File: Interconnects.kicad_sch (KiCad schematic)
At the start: 8 parts, among them J101 KLDX-0202-B, J102 EBWA-02-B, J103 EBWA-02-B, J104 KLDX-0202-B

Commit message: fix: bom improvements & more notes
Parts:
- TP101, TP104: footprint TestPoint:TestPoint_THTPad_2.0x2.0mm_Drill1.0mm -> RD-Testpoints:TestPoint_THTPad_1.5x1.5mm_Drill0.7mm
- TP102, TP103: footprint TestPoint:TestPoint_Pad_D1.5mm -> RD-Testpoints:TestPoint_Pad_D1.5mm
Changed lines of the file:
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@@
 			)
 		)
-		(property "Footprint" "TestPoint:TestPoint_THTPad_2.0x2.0mm_Drill1.0mm"
+		(property "Footprint" "RD-Testpoints:TestPoint_THTPad_1.5x1.5mm_Drill0.7mm"
 			(at 177.8 88.9 0)
 			(effects
@@
 			)
 		)
-		(property "Footprint" "TestPoint:TestPoint_Pad_D1.5mm"
+		(property "Footprint" "RD-Testpoints:TestPoint_Pad_D1.5mm"
 			(at 133.35 73.66 0)
 			(effects
@@
 			)
 		)
-		(property "Footprint" "TestPoint:TestPoint_THTPad_2.0x2.0mm_Drill1.0mm"
+		(property "Footprint" "RD-Testpoints:TestPoint_THTPad_1.5x1.5mm_Drill0.7mm"
 			(at 127 99.06 0)
 			(effects
@@
 			)
 		)
-		(property "Footprint" "TestPoint:TestPoint_Pad_D1.5mm"
+		(property "Footprint" "RD-Testpoints:TestPoint_Pad_D1.5mm"
 			(at 171.45 73.66 0)
 			(effects

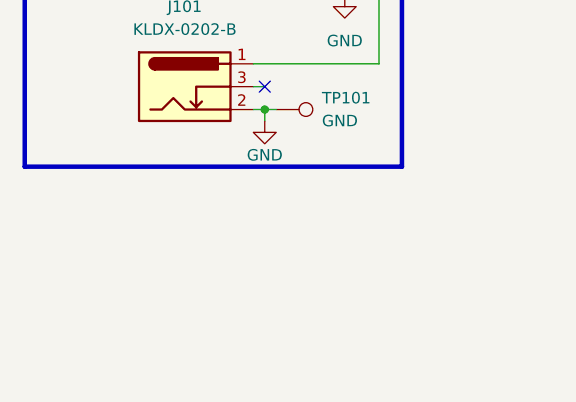
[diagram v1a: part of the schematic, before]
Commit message: feat: ERC/DRC checks
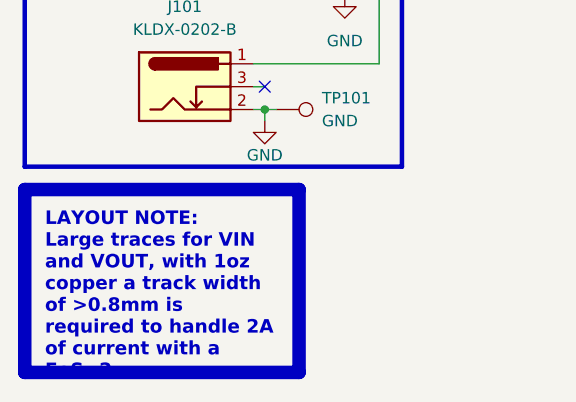
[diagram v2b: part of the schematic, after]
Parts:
- J103: Manufacturer (none) -> Adam Tech
- J104: Manufacturer (none) -> Kycon Inc

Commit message: feat!: added OC protection, redesigned board from near scratch, size increase
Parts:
- TP102, TP103: footprint RD-Testpoints:TestPoint_Pad_D1.5mm -> RD-Testpoints:TestPoint_Pad_D1.0mm
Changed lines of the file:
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@@
 			)
 		)
-		(property "Footprint" "RD-Testpoints:TestPoint_Pad_D1.5mm"
+		(property "Footprint" "RD-Testpoints:TestPoint_Pad_D1.0mm"
 			(at 133.35 73.66 0)
 			(effects
@@
 			)
 		)
-		(property "Footprint" "RD-Testpoints:TestPoint_Pad_D1.5mm"
+		(property "Footprint" "RD-Testpoints:TestPoint_Pad_D1.0mm"
 			(at 171.45 73.66 0)
 			(effects

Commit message: fix: fab layer clean up and bom additions
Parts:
- J103: MPN (none) -> EBWA-02-B
- J104: MPN (none) -> KLDX-0202-B
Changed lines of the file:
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@@
+			)
+		)
+		(property "MPN" "EBWA-02-B"
+			(at 177.8 78.74 0)
+			(effects
+				(font
+					(size 1.27 1.27)
+				)
+				(hide yes)
 			)
 		)
@@
 			(at 187.96 91.44 0)
 			(effects
+				(font
+					(size 1.27 1.27)
+				)
+				(hide yes)
+			)
+		)
+		(property "MPN" "KLDX-0202-B"
+			(at 187.96 91.44 0)
+			(effects
